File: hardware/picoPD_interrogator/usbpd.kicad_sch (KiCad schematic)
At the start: 35 parts, among them Q1 rohm-RE1C002UN, Q2 rohm-RE1C002UN, Q3 rohm-RE1C002UN, Q4 rohm-RE1C002UN, U2 ST-LM393QT

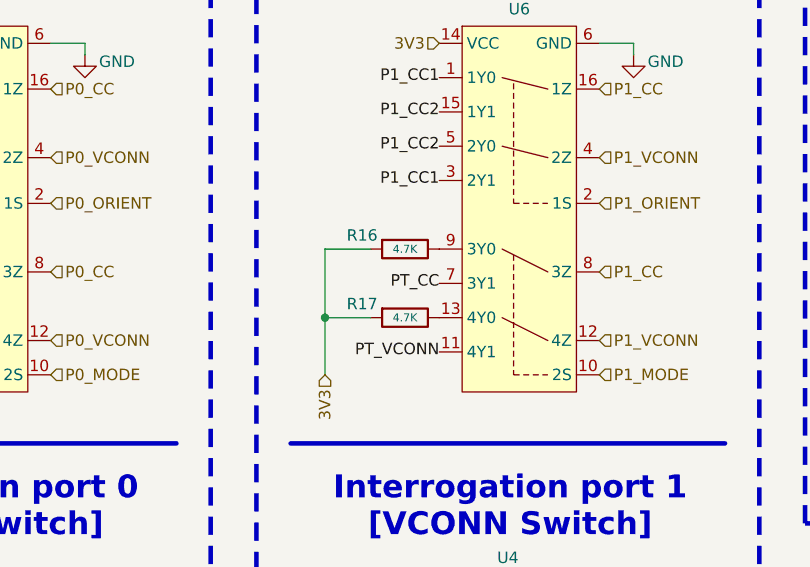
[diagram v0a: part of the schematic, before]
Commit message: Schematic: Changed Port 1 Rp value to 56K - indicating only 500ma of current can be drawn by a downstream device without a PD contract.
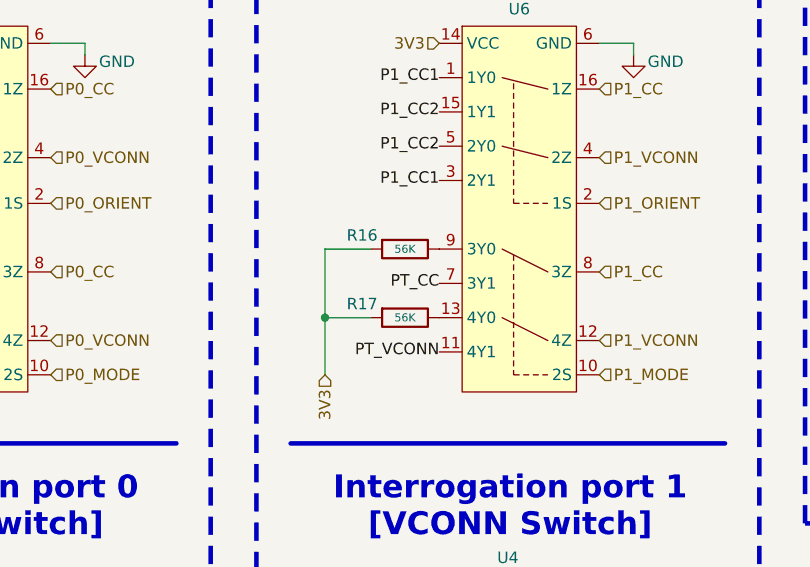
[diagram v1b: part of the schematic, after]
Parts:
- R16, R17: value 4.7K -> 56K
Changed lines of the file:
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@@
 			)
 		)
-		(property "Value" "4.7K"
+		(property "Value" "56K"
 			(at 93.98 116.84 90)
 			(effects
@@
 			)
 		)
-		(property "Value" "4.7K"
+		(property "Value" "56K"
 			(at 93.98 124.46 90)
 			(effects

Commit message: Schematic: Added QWIIC Connector. Changed 56K Rp resistor to 35K since we are pulling up 3.3v instead of 5v.
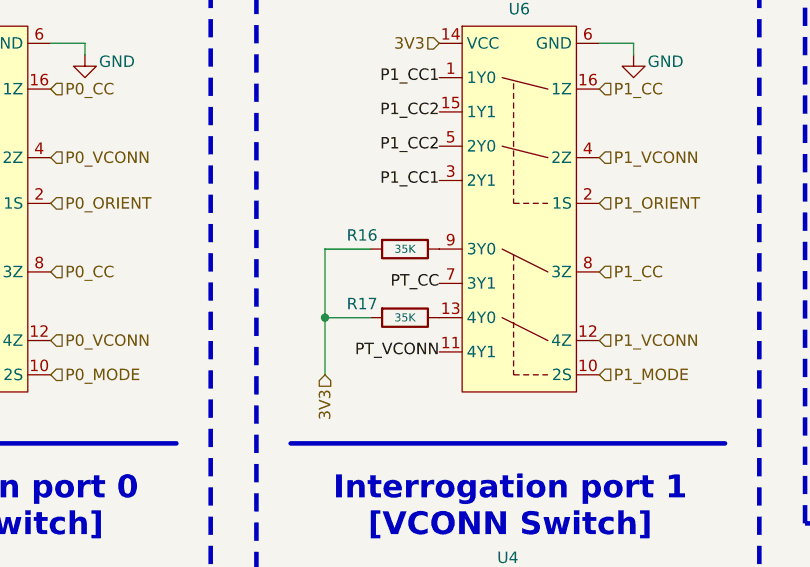
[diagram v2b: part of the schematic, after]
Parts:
- R16, R17: value 56K -> 35K
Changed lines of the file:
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@@
 			)
 		)
-		(property "Value" "56K"
+		(property "Value" "35K"
 			(at 93.98 116.84 90)
 			(effects
@@
 			)
 		)
-		(property "Value" "56K"
+		(property "Value" "35K"
 			(at 93.98 124.46 90)
 			(effects

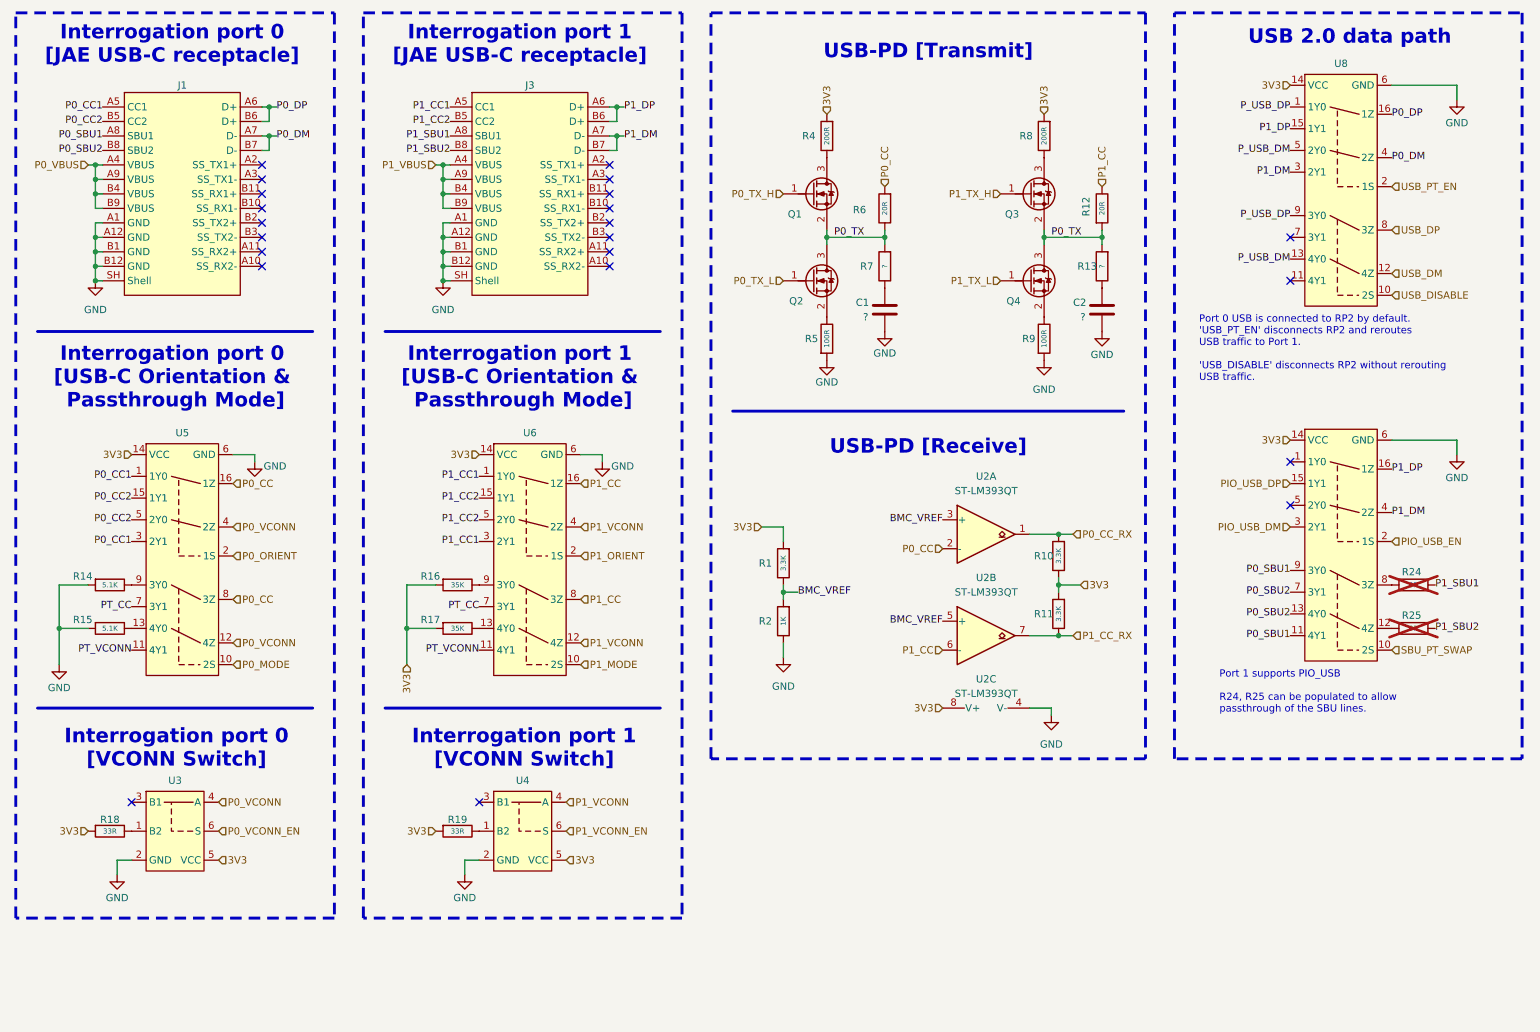
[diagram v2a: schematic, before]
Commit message: Schematic: Added VBUS Terminal Block connector & Warning message.
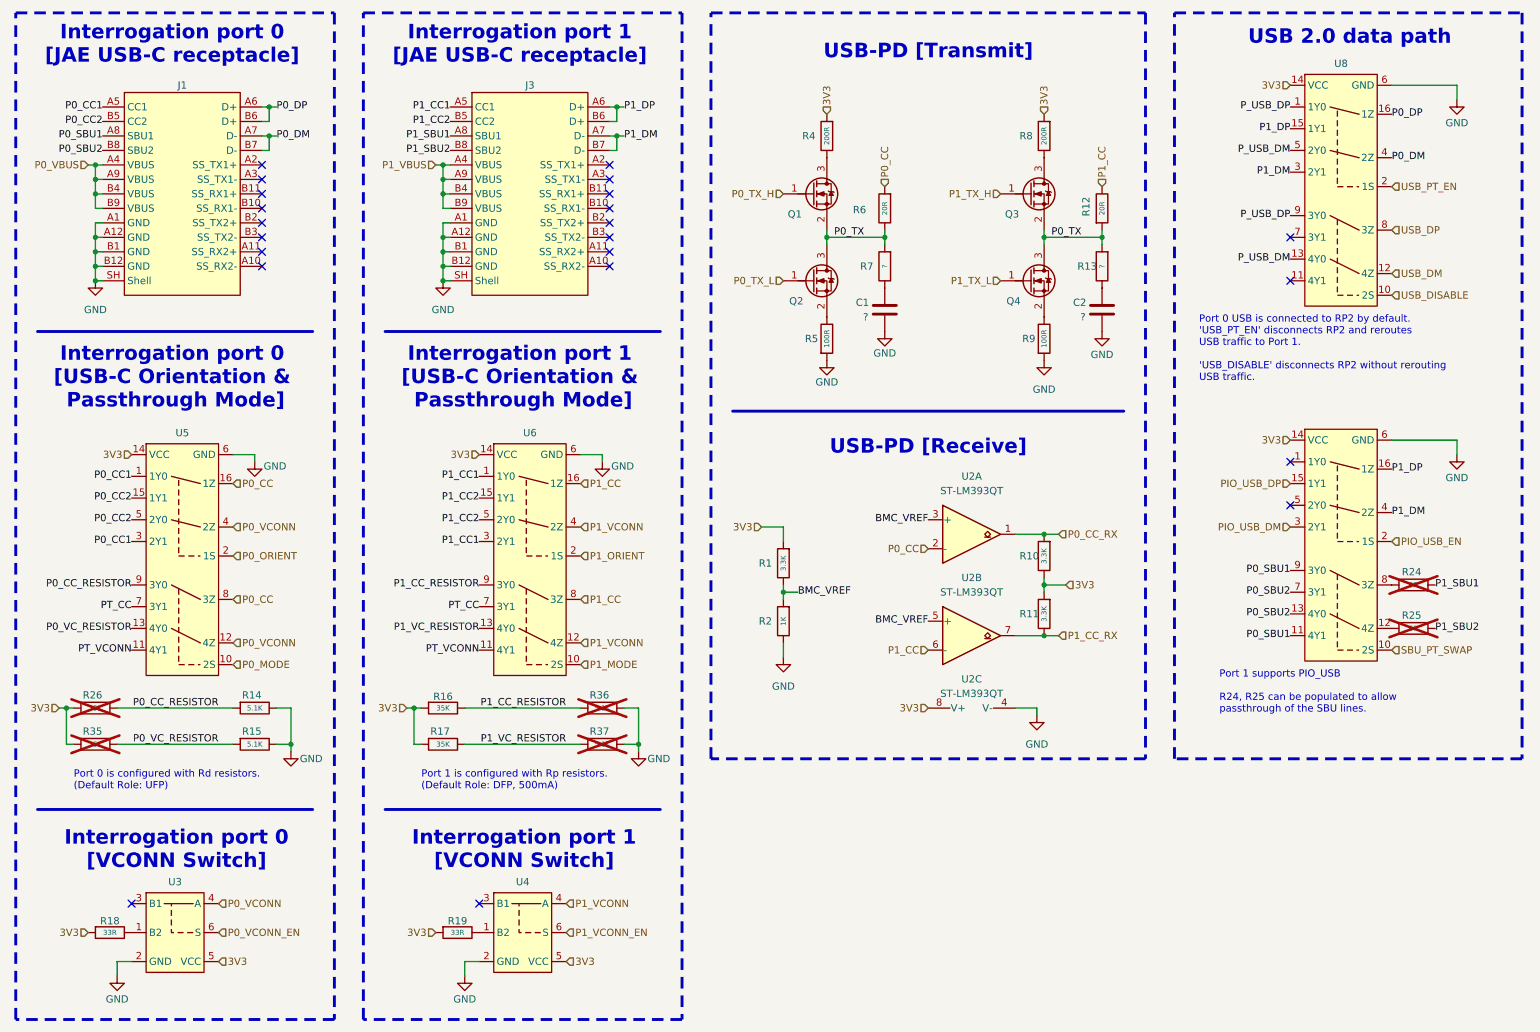
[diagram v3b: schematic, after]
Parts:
- added R26, R35: 35K, Resistor_SMD:R_0201_0603Metric, symbol Device:R
- added R36, R37: 5.1K, Resistor_SMD:R_0201_0603Metric, symbol Device:R
- R24, R25: now left out of the parts list
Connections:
- net 3V3: now also R26.2, R35.2
- net GND: now also R14.1, R15.1, R36.1, R37.1; no longer R14.2, R15.2
- net P1_VC_RESISTOR: now reaches R17.1, U6.13 (4Y0)
- net P1_VC_RESISTOR: now also R37.2
- net P1_CC_RESISTOR: now reaches R16.1, U6.9 (3Y0)
- net P1_CC_RESISTOR: now also R36.2
- net P0_VC_RESISTOR: now reaches U5.13 (4Y0)
- net P0_VC_RESISTOR: now also R15.2, R35.1; no longer R15.1
- net P0_CC_RESISTOR: now reaches U5.9 (3Y0)
- net P0_CC_RESISTOR: now also R14.2, R26.1; no longer R14.1
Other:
- note added: "Port 0 is configured with Rd resistors. (Default Role: UFP)"
- note added: "Port 1 is configured with Rp resistors. (Default Role: DFP, 500mA)"
- moved on the sheet: R10, R11, R14, R15, R16, R17, R18, R19, U2A, U2B, U2C, U3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

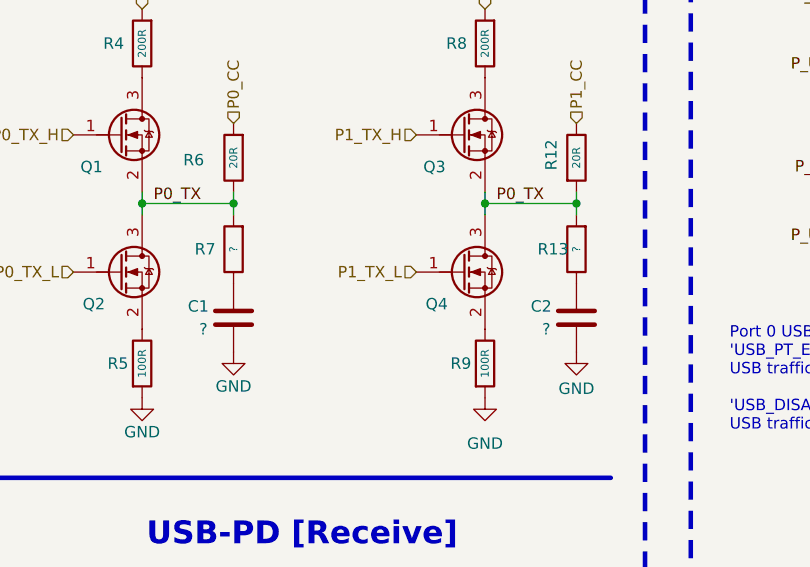
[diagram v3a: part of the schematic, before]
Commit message: Schematic: Marked some filtering passives as DNP. Annotated schematic.
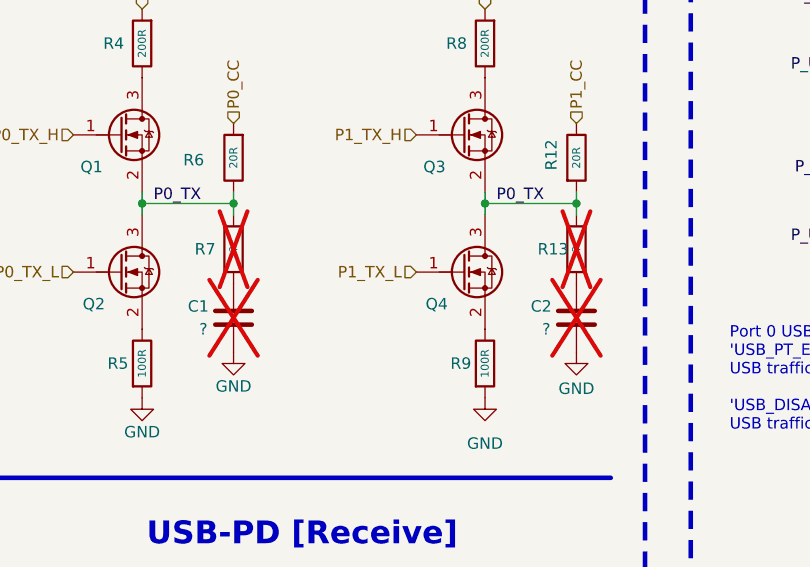
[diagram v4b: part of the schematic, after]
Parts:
- C1, C2, R13, R7: now not fitted; now left out of the parts list
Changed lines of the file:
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@@
 		(unit 1)
 		(exclude_from_sim no)
-		(in_bom yes)
-		(on_board yes)
-		(dnp no)
+		(in_bom no)
+		(on_board yes)
+		(dnp yes)
 		(property "Reference" "R13"
 			(at 202.692 60.96 0)
@@
 		(unit 1)
 		(exclude_from_sim no)
-		(in_bom yes)
-		(on_board yes)
-		(dnp no)
+		(in_bom no)
+		(on_board yes)
+		(dnp yes)
 		(property "Reference" "C1"
 			(at 163.83 67.31 0)
@@
 		(unit 1)
 		(exclude_from_sim no)
-		(in_bom yes)
-		(on_board yes)
-		(dnp no)
+		(in_bom no)
+		(on_board yes)
+		(dnp yes)
 		(property "Reference" "C2"
 			(at 201.93 67.31 0)
@@
 		(unit 1)
 		(exclude_from_sim no)
-		(in_bom yes)
-		(on_board yes)
-		(dnp no)
+		(in_bom no)
+		(on_board yes)
+		(dnp yes)
 		(property "Reference" "R7"
 			(at 164.592 60.96 0)

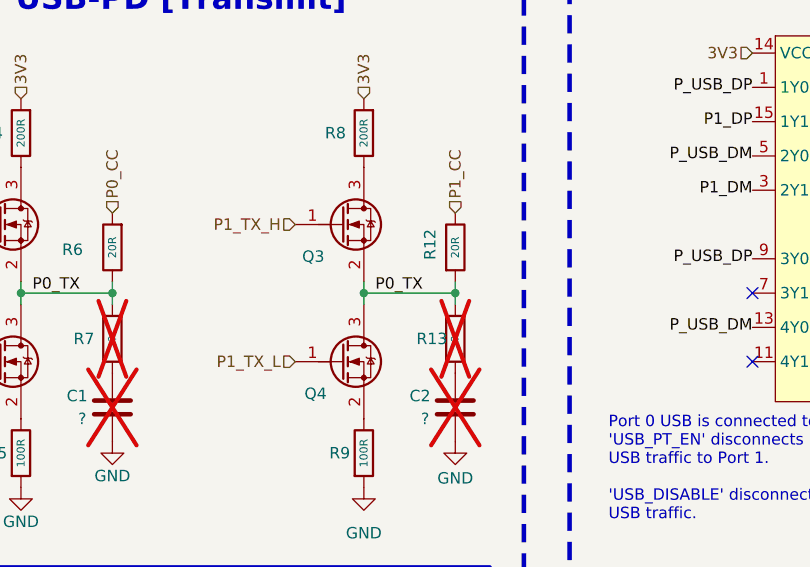
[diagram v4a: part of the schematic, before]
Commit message: Routed almost everything. Just need to finish VBUS tracks and check for any obvious issues.
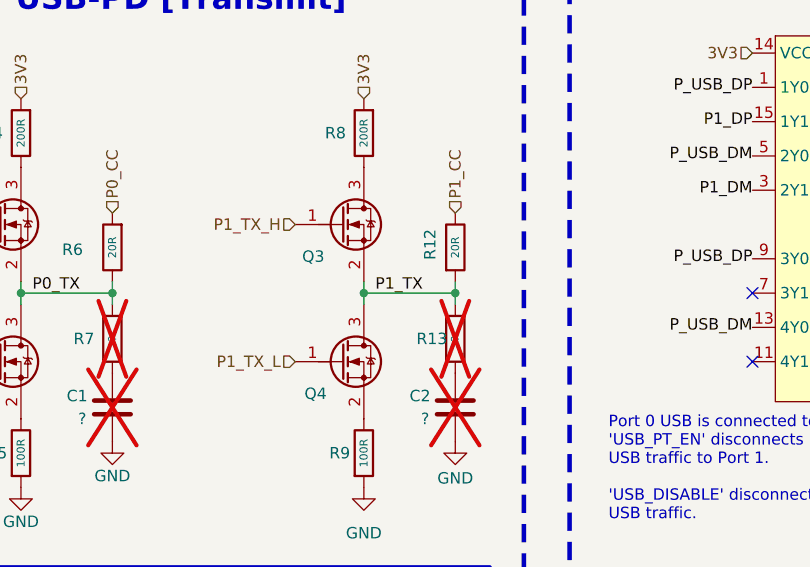
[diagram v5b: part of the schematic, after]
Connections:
- net P0_TX: no longer Q3.2 (S), Q4.3 (D), R12.2, R13.2
- new net P1_TX: Q3.2 (S), Q4.3 (D), R12.2, R13.2
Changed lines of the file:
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@@
 		)
 	)
-	(label "P0_TX"
+	(label "P1_TX"
 		(at 198.12 55.88 0)
 		(fields_autoplaced yes)
